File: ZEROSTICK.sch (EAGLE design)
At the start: 47 parts, among them IC1 ATMEGA32U4NT-TQFP, IC2 HX711-SOP16L, J1 RJ10-WURTH, J2 AUDIO-JACK-PJ321, J3 USB-C-16P-16P, K1 HE721C-DIP, Q1 2N7002, Q2 2N3906, SW1 SWITCH-SPDT-4TABSSMT, SW2 SWITCH-SPDT-4TABSSMT, SW3 RESET, SW4 Trigger Level, SW5 Tare

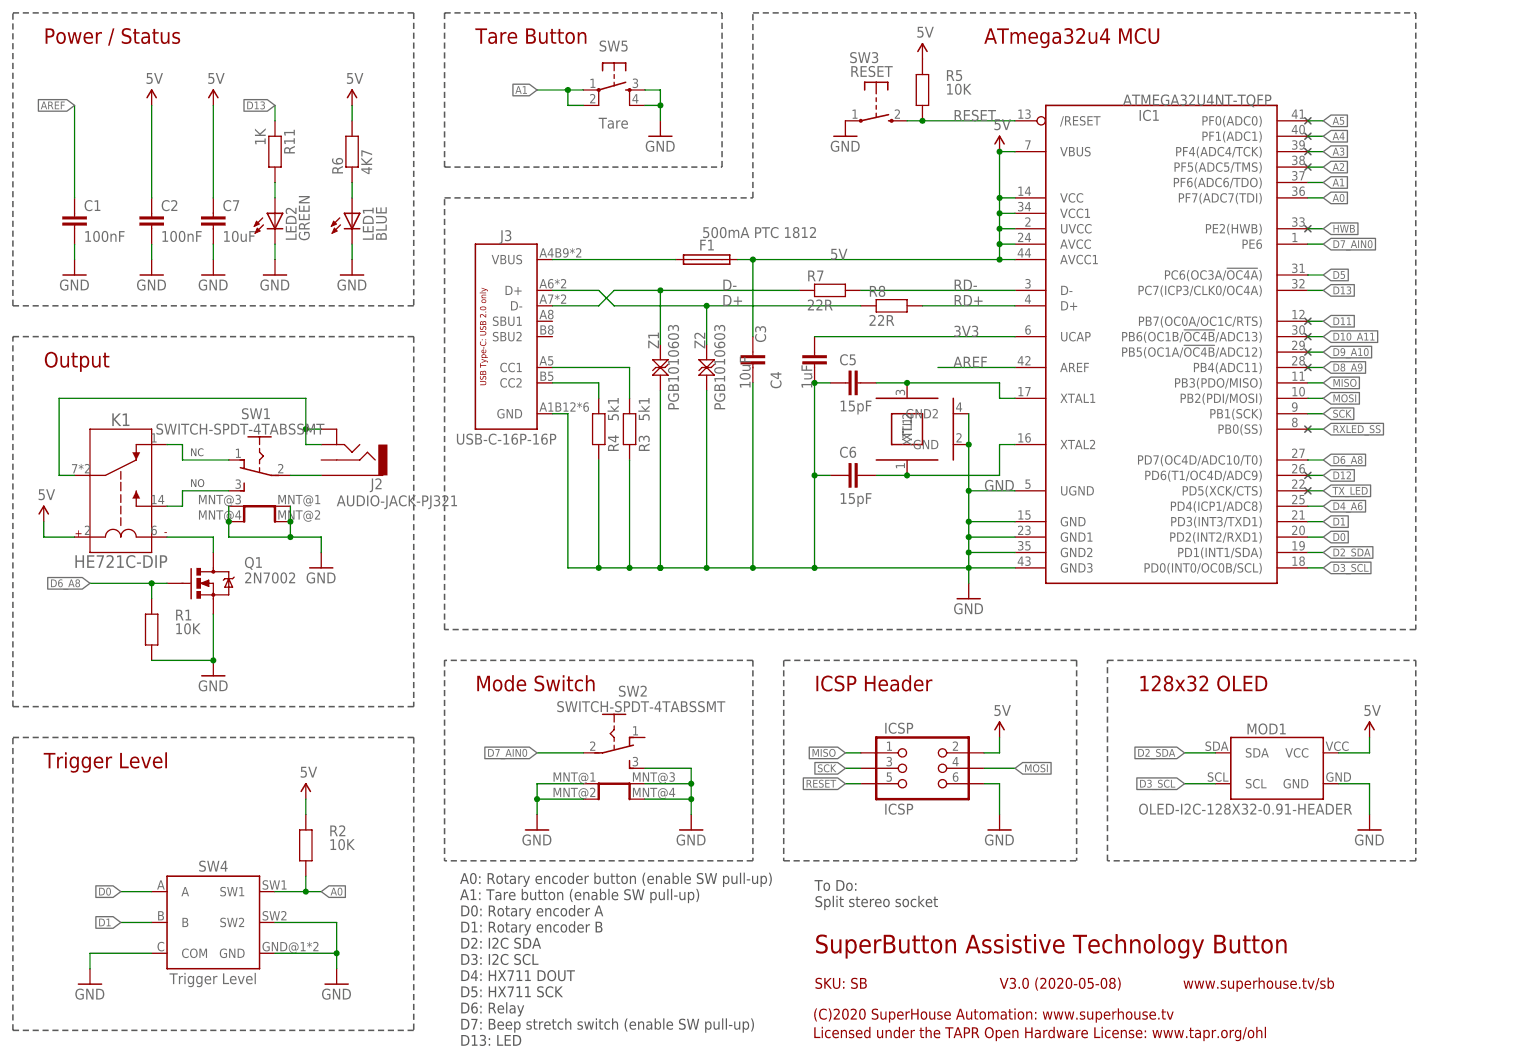
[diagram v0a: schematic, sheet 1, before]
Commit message: Partical conversion from SB project
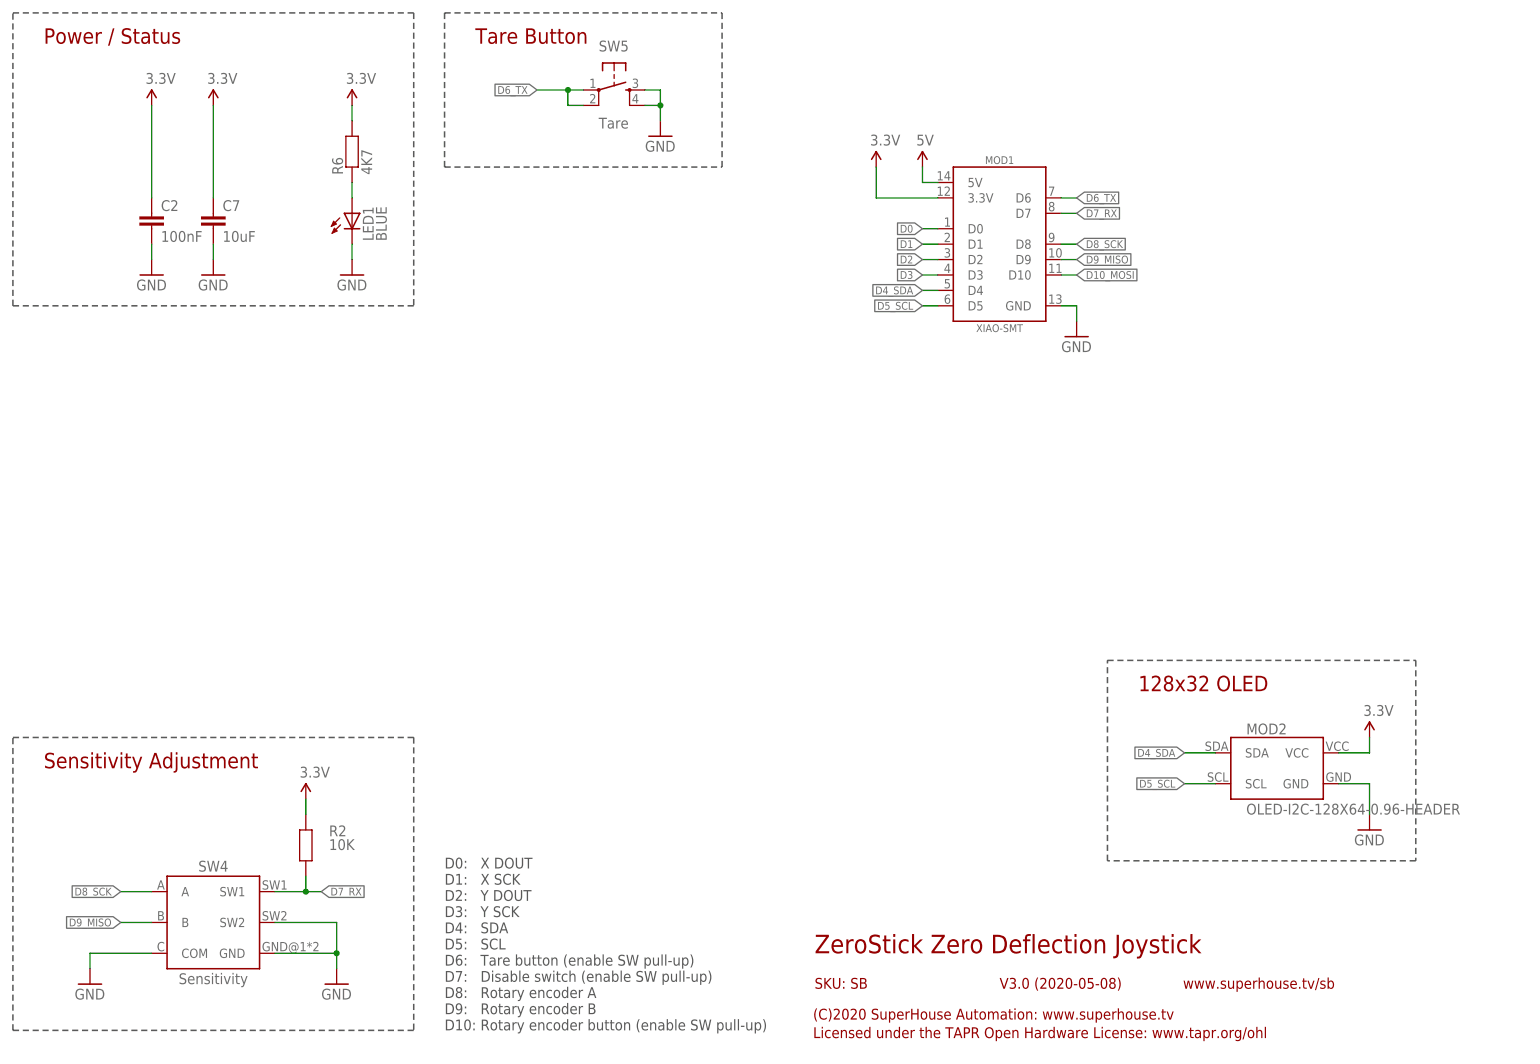
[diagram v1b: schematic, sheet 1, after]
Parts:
- removed F1: 500mA PTC 1812, SuperHouse-Fuses:PTC050
- removed ICSP: ICSP, SuperHouse-Connectors:ICSP-PIN
- removed J1: RJ10-WURTH, SuperHouse-Connectors:RJ10-WURTH
- removed J2: AUDIO-JACK-PJ321, SuperHouse-Connectors:AUDIO-JACK-PJ321
- removed J3: USB-C-16P-16P, SuperHouse-Connectors:USB-C-16P-16P
- removed K1: HE721C-DIP, SuperHouse-Relays:HE721C-DIP
- removed LED2: GREEN, SuperHouse-LEDs:LED0603
- removed R11: 1K, SuperHouse-DiscreteSemi:RESISTOR0603
- removed R7, R8: 22R, SuperHouse-DiscreteSemi:RESISTOR0603
- removed SW1, SW2: SWITCH-SPDT-4TABSSMT, SuperHouse-Switches:SWITCH-SPDT-4TABSSMT
- removed SW3: RESET, SuperHouse-Switches:TAC_SWITCH_2PINSMT
- removed XTL1: 16MHz, SuperHouse-Oscillators:CRYSTAL-GND3X2
- removed Z1, Z2: PGB1010603, SuperHouse-DiscreteSemi:TVS0603
- added L2: 3.3uH, SuperHouse-DiscreteSemi:INDUCTOR0603
- added MOD2: OLED-I2C-128X64-0.96-HEADER, SuperHouse-Displays:OLED-I2C-128X64-0.96-HEADER
- C3: value 10uF -> 100nF; device SuperHouse-DiscreteSemi:CAP0805 -> SuperHouse-DiscreteSemi:CAP0603
- C4: value 1uF -> 10uF; device SuperHouse-DiscreteSemi:CAP0603 -> SuperHouse-DiscreteSemi:CAP0805
- C5: value 15pF -> 100nF
- C6: value 15pF -> 10uF; device SuperHouse-DiscreteSemi:CAP0603 -> SuperHouse-DiscreteSemi:CAP0805
- IC1: value ATMEGA32U4NT-TQFP -> HX711-SOP16L; device SuperHouse-MCUs:ATMEGA32U4NT-TQFP -> SuperHouse-ICs:HX711-SOP16L
- MOD1: value OLED-I2C-128X32-0.91-HEADER -> XIAO-SMT; device SuperHouse-Displays:OLED-I2C-128X32-0.91-HEADER -> SuperHouse-Modules:XIAO-SMT
- Q1: value 2N7002 -> 2N3906; device SuperHouse-DiscreteSemi:MOSFET-NCHANNEL-233 -> SuperHouse-DiscreteSemi:TRANS_PNPMMBT3906LT1SOT23-BEC
- R1: value 10K -> 100R
- R3: value 5k1 -> 100R
- R4: value 5k1 -> 10K
- R5: value 10K -> 8K2
- SW4: value Trigger Level -> Sensitivity
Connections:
- removed net 3V3: C4.2, IC1.UCAP
- removed net A+: J1.3, R10.1
- removed net A-: J1.4, R9.1
- removed net A0: IC1.PF7(ADC7(TDI), R2.1, SW4.SW1
- removed net A1: IC1.PF6(ADC6/TDO), SW5.1, SW5.2
- removed net A2: IC1.PF5(ADC5/TMS)
- removed net A3: IC1.PF4(ADC4/TCK)
- removed net A4: IC1.PF1(ADC1)
- removed net A5: IC1.PF0(ADC0)
- removed net AREF: C1.1, IC1.AREF
- removed net D+: J3.D+, R8.1, Z2.2
- removed net D-: J3.D-, R7.1, Z1.2
- removed net D10_A11: IC1.PB6(OC1B/!OC4B!/ADC13)
- removed net D11: IC1.PB7(OC0A/OC1C/RTS)
- removed net D12: IC1.PD6(T1/OC4D/ADC9)
- removed net D13: IC1.PC7(ICP3/CLK0/OC4A), R11.1
- removed net D2_SDA: IC1.PD1(INT1/SDA), MOD1.SDA
- removed net D3_SCL: IC1.PD0(INT0/OC0B/SCL), MOD1.SCL
- removed net D4_A6: IC1.PD4(ICP1/ADC8), IC2.PD_SCK
- removed net D5: IC1.PC6(OC3A/!OC4A!), IC2.DOUT
- removed net D6_A8: IC1.PD7(OC4D/ADC10/T0), Q1.G, R1.2
- removed net D7_AIN0: IC1.PE6, SW2.COM
- removed net D8_A9: IC1.PB4(ADC11)
- removed net D9_A10: IC1.PB5(OC1A/!OC4B!/ADC12)
- removed net E+: C10.1, C11.1, J1.1, L1.1
- removed net HWB: IC1.PE2(HWB)
- removed net MISO: IC1.PB3(PDO/MISO), ICSP.1
- removed net MOSI: IC1.PB2(PDI/MOSI), ICSP.4
- removed net N$10: J3.CC2, R4.2
- removed net N$11: C5.2, IC1.XTAL1, XTL1.XTL2
- removed net N$12: C6.2, IC1.XTAL2, XTL1.XTL1
- removed net N$13: J3.CC1, R3.2
- removed net N$9: J2.3, SW1.COM
- removed net RD+: IC1.D+, R8.2
- removed net RD-: IC1.D-, R7.2
- removed net RESET: IC1./RESET, ICSP.5, R5.1, SW3.S
- removed net RXLED_SS: IC1.PB0(SS)
- removed net SCK: IC1.PB1(SCK), ICSP.3
- removed net TX_LED: IC1.PD5(XCK/CTS)
- removed net USB+: F1.1, J3.VBUS
- new net 3.3V: C12.1, C2.1, C6.1, C7.1, IC1.DVDD, IC1.VSUP, IC2.DVDD, IC2.VSUP, MOD1.3.3V, MOD2.VCC, Q1.E, Q2.E, R2.2, R6.2
- new net D10_MOSI: MOD1.D10
- new net D2: IC1.DOUT, MOD1.D2
- new net D3: IC1.PD_SCK, MOD1.D3
- new net D4_SDA: MOD1.D4, MOD2.SDA
- new net D5_SCL: MOD1.D5, MOD2.SCL
- new net D6_TX: MOD1.D6, SW5.1, SW5.2
- new net D7_RX: MOD1.D7, R2.1, SW4.SW1
- new net D8_SCK: MOD1.D8, SW4.A
- new net D9_MISO: MOD1.D9, SW4.B
- new net N$2: C3.2, IC1.INA+, R3.2
- new net X_A+: R10.1
- new net X_A-: R9.1
- new net X_E+: C10.1, C11.1, L1.1
- new net Y_A+: R3.1
- new net Y_A-: R1.1
- new net Y_E+: C4.1, C5.1, L2.1
- net 5V: now also MOD1.5V; no longer C12.1, C2.1, C3.1, C7.1, F1.2, IC1.AVCC, IC1.AVCC1, IC1.UVCC, IC1.VBUS, IC1.VCC, IC1.VCC1, IC2.DVDD, IC2.VSUP, ICSP.2, K1.COIL+, MOD1.VCC, Q2.E, R2.2, R5.2, R6.2
- net D0: now also IC2.DOUT, MOD1.D0; no longer IC1.PD2(INT2/RXD1), SW4.A
- net D1: now also IC2.PD_SCK, MOD1.D1; no longer IC1.PD3(INT3/TXD1), SW4.B
- net GND: now also C4.2, C5.2, C6.2, IC1.AGND, IC1.RATE, IC1.XI, MOD2.GND, R5.1; no longer C3.2, C4.1, C5.1, C6.1, IC1.GND, IC1.GND1, IC1.GND2, IC1.GND3, IC1.UGND, ICSP.6, J1.2, J3.GND, LED2.C, Q1.S, R1.1, R3.1, R4.1, SW1.MNT@1, SW1.MNT@2, SW1.MNT@3, SW1.MNT@4, SW2.B, SW2.MNT@1, SW2.MNT@2, SW2.MNT@3, SW2.MNT@4, SW3.P, XTL1.GND, XTL1.GND2, Z1.1, Z2.1
- net N$1: now also C3.1, IC1.INA-, R1.2; no longer LED2.A, R11.2
- net N$3: now also C1.1, IC1.VBG; no longer K1.COIL-, Q1.D
- net N$4: now also IC1.BASE, Q1.B; no longer K1.NO, SW1.B
- net N$6: now also IC1.VFB, R4.1, R5.2; no longer K1.NC, SW1.A
- net N$7: now also IC1.AVDD, L2.2, Q1.C, R4.2; no longer J2.4A, J2.4B, K1.COM
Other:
- note added: "D0: X DOUT D1: X SCK D2: Y DOUT D3: Y SCK D4: SDA D5: SCL D6: Tare button (enable SW pull-up) D7: Disable switch (enable SW pull-up) D8: Rotary encoder A D9: Rotary encoder B D10: Rotary encoder button (enable SW pull-up)"
- note added: "Sensitivity Adjustment"
- note added: "X Axis Load Cell Amplifier"
- note added: "Y Axis Load Cell Amplifier"
- note added: "ZeroStick Zero Deflection Joystick"
- note removed: "A0: Rotary encoder button (enable SW pull-up) A1: Tare button (enable SW pull-up) D0: Rotary encoder A D1: Rotary encoder B D2: I2C SDA D3: I2C SCL D4: HX711 DOUT D5: HX711 SCK D6: Relay D7: Beep stretch switch (enable SW pull-up) D13: LED"
- note removed: "ATmega32u4 MCU"
- note removed: "ICSP Header"
- note removed: "Load Cell Amplifier"
- note removed: "Mode Switch"
- note removed: "NC"
- note removed: "NO"
- note removed: "Output"
- note removed: "SuperButton Assistive Technology Button"
- note removed: "To Do: Split stereo socket"
- note removed: "Trigger Level"
